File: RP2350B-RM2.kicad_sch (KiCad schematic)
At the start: 60 parts, among them J1 10103594-0001LF, J2 TSW-126-07-L-D, J3 TSW-126-07-L-D, J4 SM03B-SRSS-TB(LF)(SN), SW1 434133025816, SW2 434133025816, U1 RP2350B, U2 NCP1117ST33T3G, U3 W25Q128JVSIQ, U4 APS6404L-3SQR-SN, U5 RM2, X1 12MHz

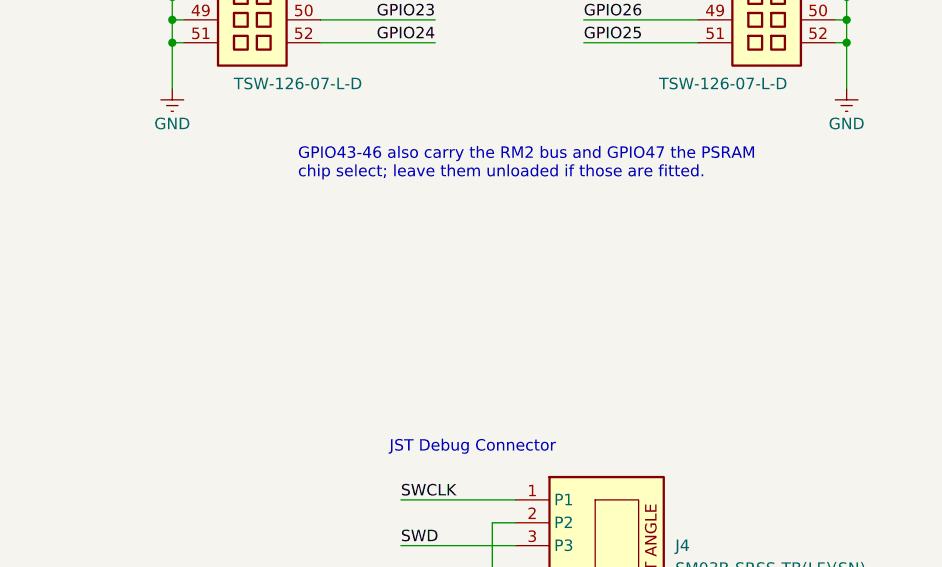
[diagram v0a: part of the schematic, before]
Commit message: Add 3V3 header extensions J5/J6 and move the bottom mounting holes
Schematic: add J5 and J6, 2x02 headers that continue J2 and J3 by two
rows. Each has two 3V3 pins on the inner column and two GND pins on the
outer column, matching how J2/J3 are laid out. New footprint
PinHeader_2x02_P2.54mm_Ext: round pads, with silkscreen that joins the
header outline above.

Board: J5/J6 sit on J2/J3's 2.54 mm grid with "3V3" labels in Pi's
style. The WL_ON and CS lanes now turn below them, and J6's 3V3 pins get
a track into the pour. MH3/MH4 move to the new end, in line with the top
pair and 4 mm from the edge, so the holes form a 27.94 x 81.5 mm
rectangle. The antenna rule area allows the NPTH holes.

DRC: 0 unconnected items, 0 parity issues; only Pi's RPI_COMPILED
library notes. ERC: unchanged (4 pre-existing items).

Co-Authored-By: Claude Opus 5.5 <noreply@anthropic.com>
Claude-Session: https://claude.ai/code/session_01TVxWe2rd4mhh6Q8D57QZer
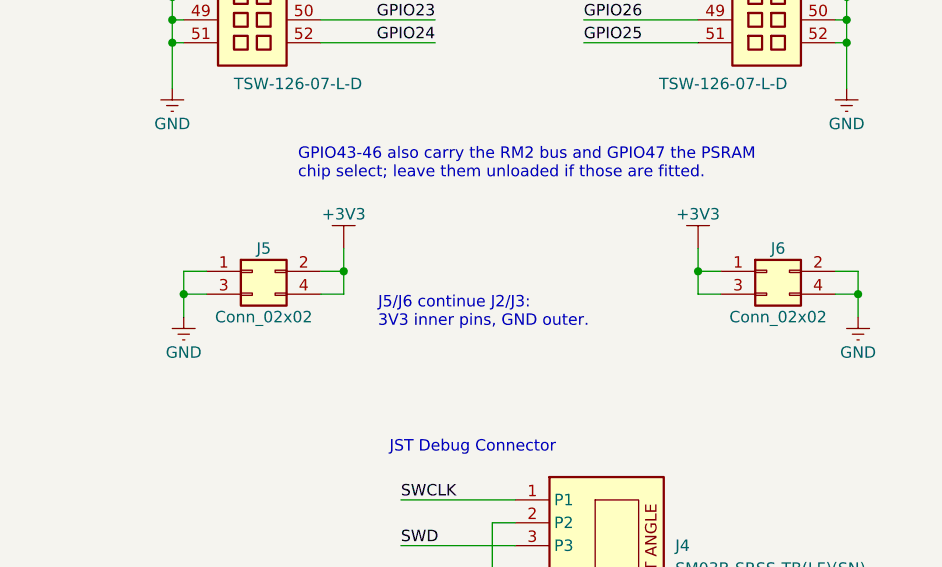
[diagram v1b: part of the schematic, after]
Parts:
- added J5, J6: Conn_02x02, rp2350b_rm2:PinHeader_2x02_P2.54mm_Ext, symbol Connector_Generic:Conn_02x02_Odd_Even
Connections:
- net +3V3: now also J5.2 (Pin_2), J5.4 (Pin_4), J6.1 (Pin_1), J6.3 (Pin_3)
- net GND: now also J5.1 (Pin_1), J5.3 (Pin_3), J6.2 (Pin_2), J6.4 (Pin_4)
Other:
- note added: "J5/J6 continue J2/J3: 3V3 inner pins, GND outer."

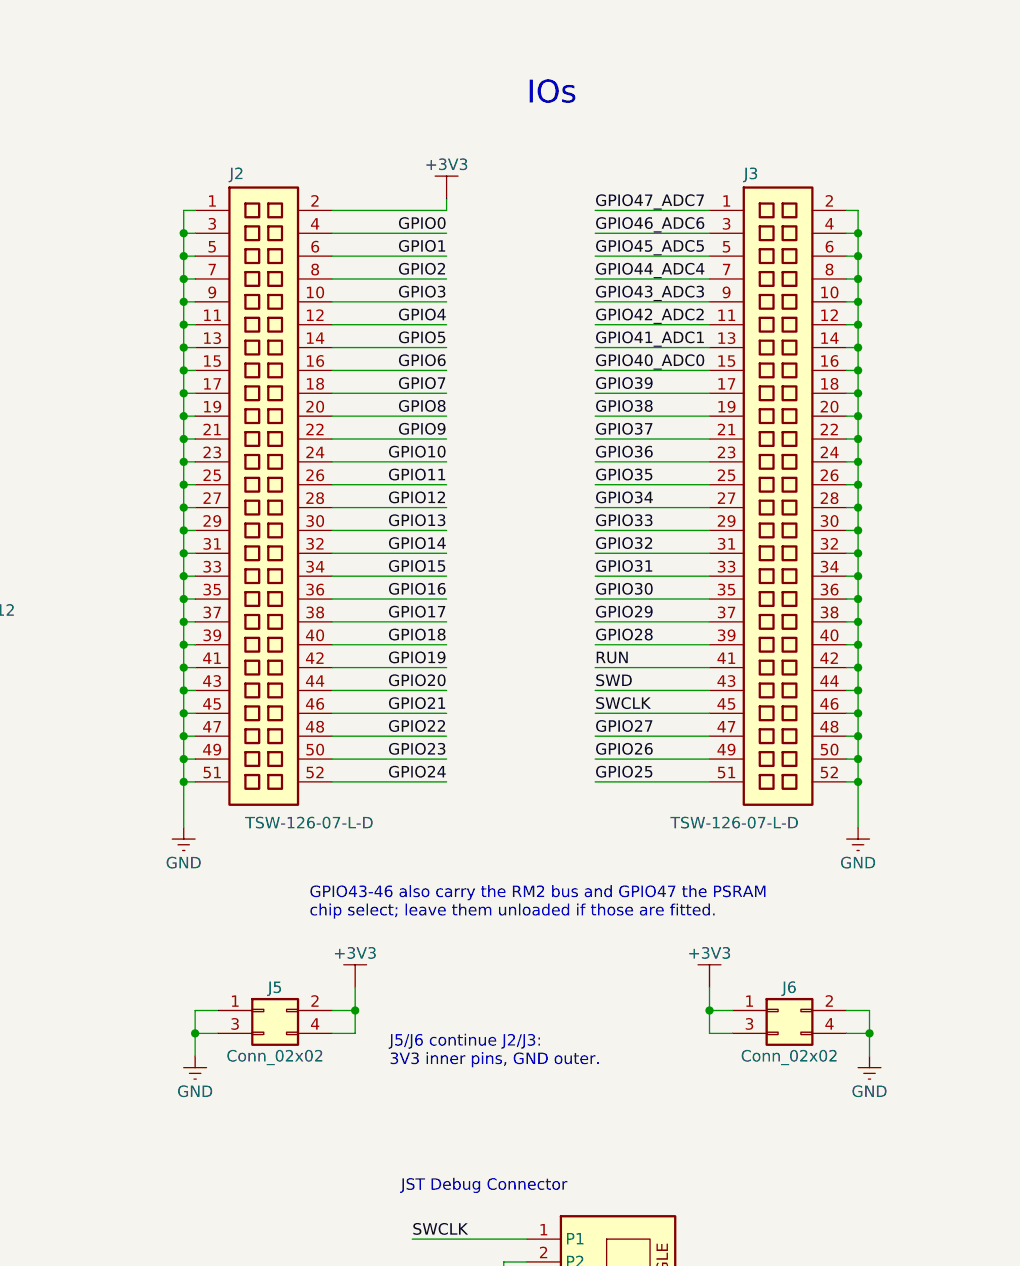
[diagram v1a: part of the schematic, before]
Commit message: Single-row J2/J3 headers with 3V3 and GND at the ends
Replace Pi's 2x26 headers (outer column all GND) and the J5/J6
extensions with single-row headers on Pi's signal columns:
  J2 (1x29): 3V3, GPIO0-24, GND, 3V3, GND
  J3 (1x28): 3V3, 3V3, GND x3, GPIO42-28, RUN, SWD, SWCLK,
             GPIO27-25, 3V3, GND
GPIO43-47 leave the header, since the radio and PSRAM need them.

Schematic: new Conn_01x29 / Conn_01x28 symbols sit exactly on the old
signal-pin positions, so every GPIO label connection carries over.
The GND buses, J5/J6 and the GPIO43-47 header hookups are removed.

Board: stock PinHeader_1x29/1x28 footprints on the same pads, so Pi's
routing to every GPIO is untouched. Pi's GPIO43-46 runs stop short of
J3's new power pins and slip between them into four lanes where the
outer column was. GPIO47 stops at the via to R11. J3's top 3V3 pins
join the pour by U2. Silkscreen: J3's top labels now read 3V3/GND,
"ADC 40-42", and the "Outer Row GND" notes are gone. The J5/J6
footprint is removed.

DRC: 0 unconnected items, 0 parity issues, only Pi's 46 RPI_COMPILED
library notes. ERC unchanged (4 pre-existing items). U2 to the RM2's
VIN is now about 15 mOhm, down from 19.

Co-Authored-By: Claude Opus 5.5 <noreply@anthropic.com>
Claude-Session: https://claude.ai/code/session_01TVxWe2rd4mhh6Q8D57QZer
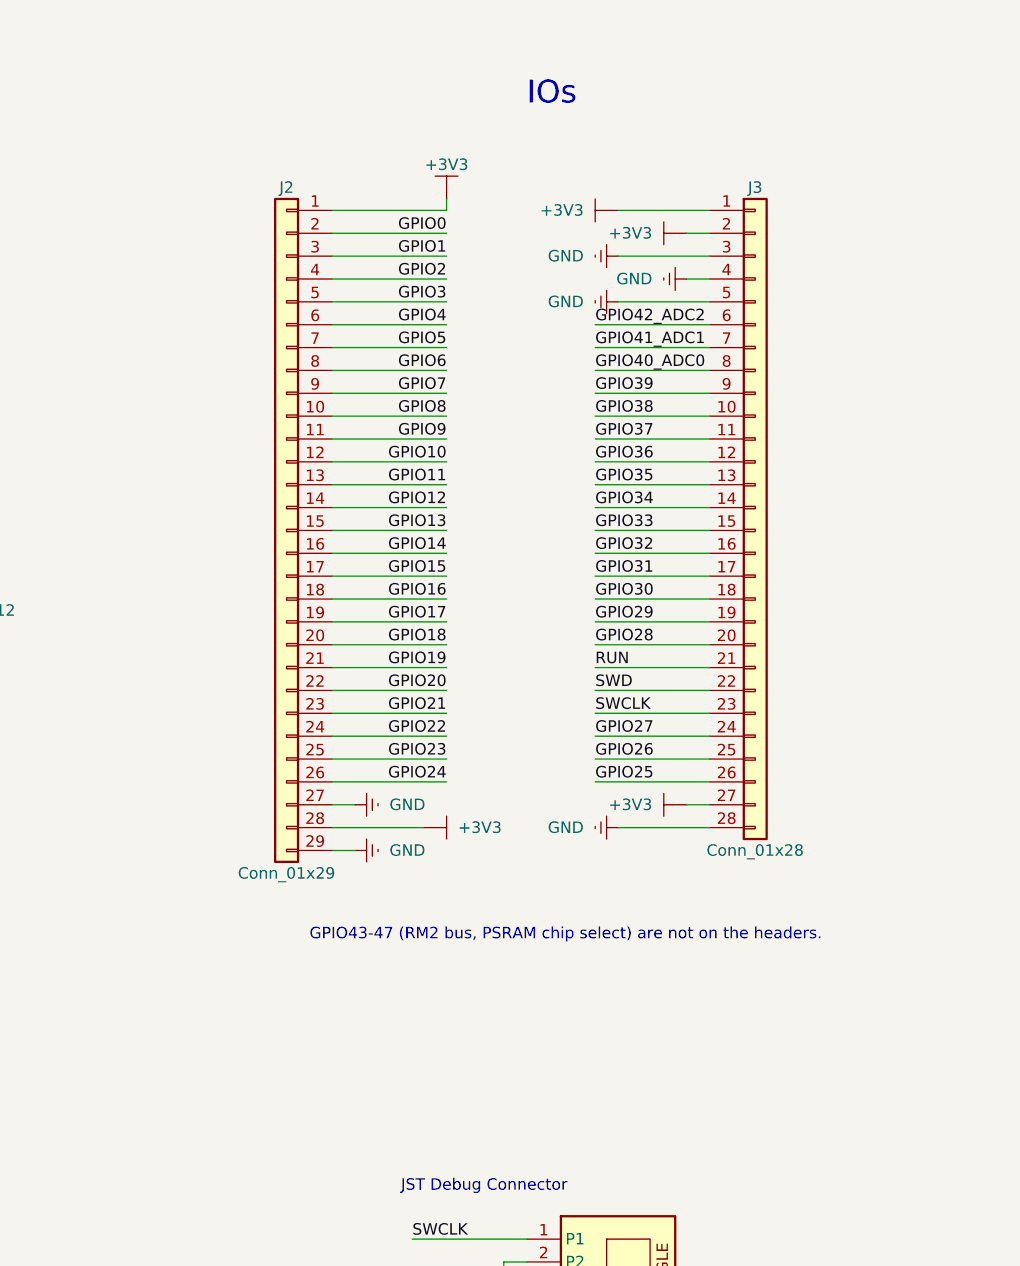
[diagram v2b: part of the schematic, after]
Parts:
- removed J2, J3: TSW-126-07-L-D, RPI_COMPILED:samtec_tsw-126-07-l-d, symbol RPI_DB:Connectors | Pin_Headers/RP-01KJ62-FD8Y6K
- removed J5, J6: Conn_02x02, rp2350b_rm2:PinHeader_2x02_P2.54mm_Ext, symbol Connector_Generic:Conn_02x02_Odd_Even
- added J2: Conn_01x29, Connector_PinHeader_2.54mm:PinHeader_1x29_P2.54mm_Vertical, symbol Connector_Generic:Conn_01x29
- added J3: Conn_01x28, Connector_PinHeader_2.54mm:PinHeader_1x28_P2.54mm_Vertical, symbol Connector_Generic:Conn_01x28
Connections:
- net +3V3: now also J2.1 (Pin_1), J2.28 (Pin_28), J3.1 (Pin_1), J3.2 (Pin_2), J3.27 (Pin_27)
- net GND: now also J2.27 (Pin_27), J2.29 (Pin_29), J3.28 (Pin_28), J3.3 (Pin_3), J3.4 (Pin_4), J3.5 (Pin_5)
- net GPIO0: now also J2.2 (Pin_2)
- net GPIO1: now also J2.3 (Pin_3)
- net GPIO10: now also J2.12 (Pin_12)
- net GPIO11: now also J2.13 (Pin_13)
- net GPIO12: now also J2.14 (Pin_14)
- net GPIO13: now also J2.15 (Pin_15)
- net GPIO14: now also J2.16 (Pin_16)
- net GPIO15: now also J2.17 (Pin_17)
- net GPIO16: now also J2.18 (Pin_18)
- net GPIO17: now also J2.19 (Pin_19)
- net GPIO18: now also J2.20 (Pin_20)
- net GPIO19: now also J2.21 (Pin_21)
- net GPIO2: now also J2.4 (Pin_4)
- net GPIO20: now also J2.22 (Pin_22)
- net GPIO21: now also J2.23 (Pin_23)
- net GPIO22: now also J2.24 (Pin_24)
- net GPIO23: now also J2.25 (Pin_25)
- net GPIO24: now also J2.26 (Pin_26)
- net GPIO25: now also J3.26 (Pin_26)
- net GPIO26: now also J3.25 (Pin_25)
- net GPIO27: now also J3.24 (Pin_24)
- net GPIO28: now also J3.20 (Pin_20)
- net GPIO29: now also J3.19 (Pin_19)
- net GPIO3: now also J2.5 (Pin_5)
- net GPIO30: now also J3.18 (Pin_18)
- net GPIO31: now also J3.17 (Pin_17)
- net GPIO32: now also J3.16 (Pin_16)
- net GPIO33: now also J3.15 (Pin_15)
- net GPIO34: now also J3.14 (Pin_14)
- net GPIO35: now also J3.13 (Pin_13)
- net GPIO36: now also J3.12 (Pin_12)
- net GPIO37: now also J3.11 (Pin_11)
- net GPIO38: now also J3.10 (Pin_10)
- net GPIO39: now also J3.9 (Pin_9)
- net GPIO4: now also J2.6 (Pin_6)
- net GPIO40_ADC0: now also J3.8 (Pin_8)
- net GPIO41_ADC1: now also J3.7 (Pin_7)
- net GPIO42_ADC2: now also J3.6 (Pin_6)
- net GPIO5: now also J2.7 (Pin_7)
- net GPIO6: now also J2.8 (Pin_8)
- net GPIO7: now also J2.9 (Pin_9)
- net GPIO8: now also J2.10 (Pin_10)
- net GPIO9: now also J2.11 (Pin_11)
- net RUN: now also J3.21 (Pin_21)
- net SWCLK: now also J3.23 (Pin_23)
- net SWD: now also J3.22 (Pin_22)
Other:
- note added: "GPIO43-47 (RM2 bus, PSRAM chip select) are not on the headers."
- note removed: "GPIO43-46 also carry the RM2 bus and GPIO47 the PSRAM chip select; leave them unloaded if those are fitted."
- note removed: "J5/J6 continue J2/J3: 3V3 inner pins, GND outer."

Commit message: Remove the J4 debug connector; route SWD/SWCLK straight to J3
SWD and SWCLK are on J3 (pins 22/23, next to RUN), so the JST debug
connector is redundant.

Schematic: J4, its wiring, its GND symbol and the "JST Debug Connector"
heading are removed. SWD/SWCLK keep their labels at U1 and J3.

Board (edited on top of the refilled board): J4, its GND stubs and two
vias, and the "DEBUG" silkscreen are removed. Pi ran SWD and SWCLK
through J4's pads; they now continue along the same 45-degree lines
into their existing horizontal runs to J3. Zones refilled.

Pipeline: update_pcb_from_sch.py now deletes footprints whose symbol is
gone, and layout_rm2.py has the matching J4 section. Re-running both from
Pi's original board reproduces this board exactly (same footprints,
tracks, vias and zones). The layout script's docstring is brought up to
date.

DRC: 0 unconnected items, 0 parity issues, 45 RPI_COMPILED library
notes. ERC unchanged (4 pre-existing items). The J4 BOM line is removed.

Co-Authored-By: Claude Opus 5.5 <noreply@anthropic.com>
Claude-Session: https://claude.ai/code/session_01TVxWe2rd4mhh6Q8D57QZer
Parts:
- removed J4: SM03B-SRSS-TB(LF)(SN), RPI_COMPILED:jst_sm03b-srss-tb-lf--sn-, symbol RPI_DB:Connectors | Rectangular/RP-01EKJ1-8V9SV1
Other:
- note removed: "JST Debug Connector"
